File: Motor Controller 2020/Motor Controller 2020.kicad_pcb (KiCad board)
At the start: 2 copper layers, 86 x 60 mm, 49 parts, among them J1 Batt+, J2 Batt-, J3 Input, J4 Motor+, J5 Motor-, Q1 IRF1404, Q2 IRF1404, Q3 IRF1404, Q4 IRF1404, SW1 SW_DIP_x03, U1 MAX15062A, U2 Attiny4313, U3 a4956

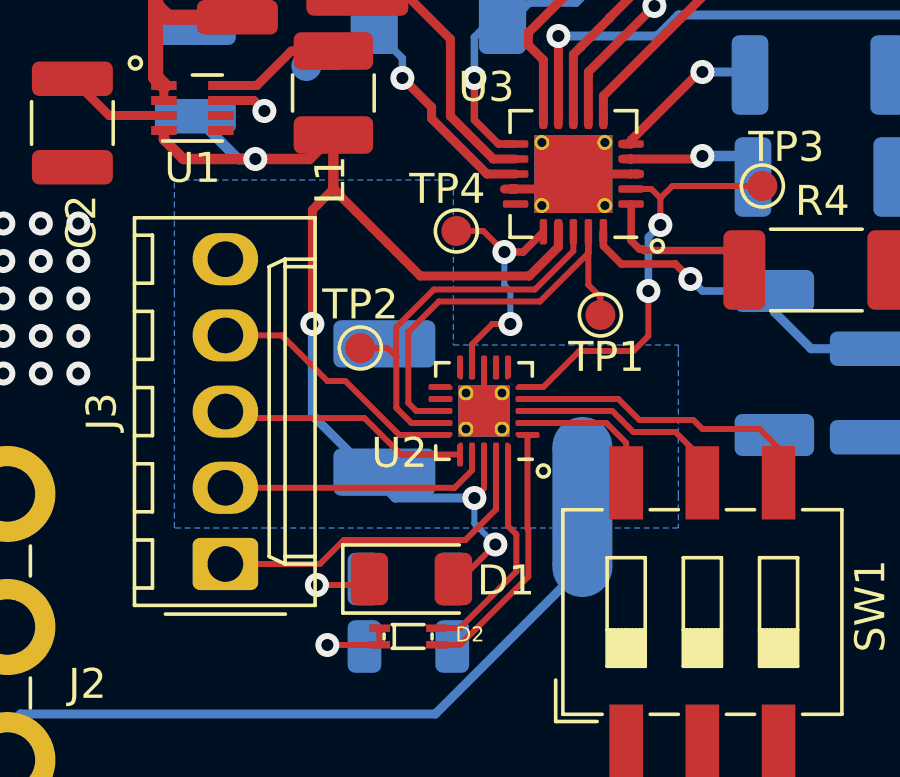
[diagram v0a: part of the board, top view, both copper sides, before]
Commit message: Created new version
Updated PCB and added CRC check for incoming data
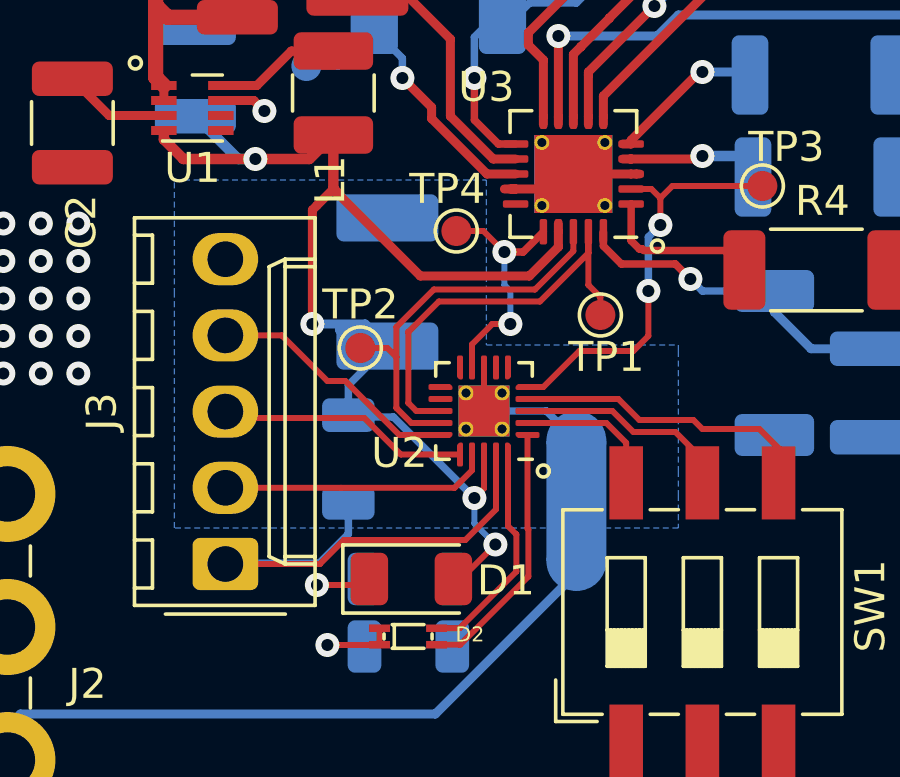
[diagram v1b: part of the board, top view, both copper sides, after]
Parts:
- added R9: 15k, Resistor_SMD:R_1206_3216Metric, B.Cu at (112.7, 89.1)
- moved C7 4.20 mm to (114.0, 83.2)
- moved NT1 0.28 mm to (120.3, 90.5)
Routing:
- net A_RESET: track 11.6 -> 17.2 mm
- net +5V: track 41.5 -> 44.6 mm
- net GNDD: track 4.27 -> 4.94 mm

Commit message: Updated PCB
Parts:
- added R10: 15k, Resistor_SMD:R_1206_3216Metric, F.Cu at (95.0, 61.1)
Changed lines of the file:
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@@
     (tracks 676)
     (zones 0)
-    (modules 50)
+    (modules 51)
     (nets 45)
   )
@@
     (0 F.Cu signal)
     (31 B.Cu signal)
-    (32 B.Adhes user)
-    (33 F.Adhes user)
-    (34 B.Paste user)
-    (35 F.Paste user)
+    (32 B.Adhes user hide)
+    (33 F.Adhes user hide)
+    (34 B.Paste user hide)
+    (35 F.Paste user hide)
     (36 B.SilkS user)
     (37 F.SilkS user)
-    (38 B.Mask user)
-    (39 F.Mask user)
+    (38 B.Mask user hide)
+    (39 F.Mask user hide)
     (40 Dwgs.User user)
     (41 Cmts.User user hide)
@@
     (pad 2 smd roundrect (at 1.4625 0 270) (size 1.125 1.75) (layers B.Cu B.Paste B.Mask) (roundrect_rratio 0.222222)
       (net 17 A_RESET))
+    (model ${KISYS3DMOD}/Resistor_SMD.3dshapes/R_1206_3216Metric.wrl
+      (at (xyz 0 0 0))
+      (scale (xyz 1 1 1))
+      (rotate (xyz 0 0 0))
+    )
+  )
+  (module Resistor_SMD:R_1206_3216Metric (layer F.Cu)
+    (at 95 61.1 270)
+    (descr "Resistor SMD 1206 (3216 Metric), square (rectangular) end terminal, IPC_7351 nominal, (Body size source: IPC-SM-782 page 72, https://www.pcb-3d.com/wordpress/wp-content/uploads/ipc-sm-782a_amendment_1_and_2.pdf), generated with kicad-footprint-generator")
+    (tags resistor)
+    (attr smd)
+    (fp_text reference R10 (at 0 -1.82 90) (layer F.SilkS)
+      (effects (font (size 1 1) (thickness 0.15)))
+    )
+    (fp_text value 15k (at 0 1.82 90) (layer F.Fab)
+      (effects (font (size 1 1) (thickness 0.15)))
+    )
+    (fp_line (start 2.28 1.12) (end -2.28 1.12) (layer F.CrtYd) (width 0.05))
+    (fp_line (start 2.28 -1.12) (end 2.28 1.12) (layer F.CrtYd) (width 0.05))
+    (fp_line (start -2.28 -1.12) (end 2.28 -1.12) (layer F.CrtYd) (width 0.05))
+    (fp_line (start -2.28 1.12) (end -2.28 -1.12) (layer F.CrtYd) (width 0.05))
+    (fp_line (start -0.727064 0.91) (end 0.727064 0.91) (layer F.SilkS) (width 0.12))
+    (fp_line (start -0.727064 -0.91) (end 0.727064 -0.91) (layer F.SilkS) (width 0.12))
+    (fp_line (start 1.6 0.8) (end -1.6 0.8) (layer F.Fab) (width 0.1))
+    (fp_line (start 1.6 -0.8) (end 1.6 0.8) (layer F.Fab) (width 0.1))
+    (fp_line (start -1.6 -0.8) (end 1.6 -0.8) (layer F.Fab) (width 0.1))
+    (fp_line (start -1.6 0.8) (end -1.6 -0.8) (layer F.Fab) (width 0.1))
+    (fp_text user %R (at 0 0 90) (layer F.Fab)
+      (effects (font (size 0.8 0.8) (thickness 0.12)))
+    )
+    (pad 1 smd roundrect (at -1.4625 0 270) (size 1.125 1.75) (layers F.Cu F.Paste F.Mask) (roundrect_rratio 0.222222)
+      (net 26 VCC))
+    (pad 2 smd roundrect (at 1.4625 0 270) (size 1.125 1.75) (layers F.Cu F.Paste F.Mask) (roundrect_rratio 0.222222)
+      (net 1 GND))
     (model ${KISYS3DMOD}/Resistor_SMD.3dshapes/R_1206_3216Metric.wrl
       (at (xyz 0 0 0))
@@
   (segment (start 116.45 93.1) (end 117.6 91.95) (width 0.2) (layer F.Cu) (net 2))
   (segment (start 116.2 93.1) (end 116.45 93.1) (width 0.2) (layer F.Cu) (net 2))
+  (segment (start 113.8 85.4625) (end 113.0625 85.4625) (width 0.3) (layer B.Cu) (net 2))
+  (segment (start 113.0625 85.4625) (end 112.4 84.8) (width 0.3) (layer B.Cu) (net 2))
+  (segment (start 113.2625 84.6) (end 114 85.3375) (width 0.3) (layer B.Cu) (net 2))
+  (segment (start 111.5 84.6) (end 113.2625 84.6) (width 0.3) (layer B.Cu) (net 2))
+  (segment (start 112.7 86.6375) (end 114 85.3375) (width 0.25) (layer B.Cu) (net 2))
+  (segment (start 112.7 87.6375) (end 112.7 86.6375) (width 0.25) (layer B.Cu) (net 2))
+  (segment (start 116.9 90.4) (end 114.2 87.7) (width 0.25) (layer B.Cu) (net 2))
+  (segment (start 112.7625 87.7) (end 112.7 87.6375) (width 0.25) (layer B.Cu) (net 2))
+  (segment (start 114.2 87.7) (end 112.7625 87.7) (width 0.25) (layer B.Cu) (net 2))
   (via (at 144.5 73.7) (size 0.8) (drill 0.4) (layers F.Cu B.Cu) (net 3))
   (via (at 119.7 75) (size 0.8) (drill 0.4) (layers F.Cu B.Cu) (net 3))
@@
   (segment (start 112.55 91.8) (end 116.6 91.8) (width 0.2) (layer F.Cu) (net 17))
   (segment (start 108.6 92.6) (end 111.75 92.6) (width 0.2) (layer F.Cu) (net 17))
+  (segment (start 112.7 90.5625) (end 112.7 91.6) (width 0.25) (layer B.Cu) (net 17))
+  (segment (start 108.625001 92.574999) (end 108.6 92.6) (width 0.25) (layer B.Cu) (net 17))
+  (segment (start 111.725001 92.574999) (end 108.625001 92.574999) (width 0.25) (layer B.Cu) (net 17))
+  (segment (start 112.7 91.6) (end 111.725001 92.574999) (width 0.25) (layer B.Cu) (net 17))
   (via (at 118.1 84.6) (size 0.8) (drill 0.4) (layers F.Cu B.Cu) (net 18))
   (via (at 117.9 82.2) (size 0.8) (drill 0.4) (layers F.Cu B.Cu) (net 18))
@@
   (segment (start 108.45 76.65) (end 109.65 76.65) (width 0.3) (layer F.Cu) (net 22))
   (segment (start 112.2 75.5) (end 110.8 75.5) (width 0.3) (layer F.Cu) (net 22))
-  (segment (start 113.8 85.4625) (end 113.0625 85.4625) (width 0.3) (layer B.Cu) (net 2))
-  (segment (start 113.0625 85.4625) (end 112.4 84.8) (width 0.3) (layer B.Cu) (net 2))
-  (segment (start 113.2625 84.6) (end 114 85.3375) (width 0.3) (layer B.Cu) (net 2))
-  (segment (start 111.5 84.6) (end 113.2625 84.6) (width 0.3) (layer B.Cu) (net 2))
-  (segment (start 112.7 86.6375) (end 114 85.3375) (width 0.25) (layer B.Cu) (net 2))
-  (segment (start 112.7 87.6375) (end 112.7 86.6375) (width 0.25) (layer B.Cu) (net 2))
-  (segment (start 116.9 90.4) (end 114.2 87.7) (width 0.25) (layer B.Cu) (net 2))
-  (segment (start 112.7625 87.7) (end 112.7 87.6375) (width 0.25) (layer B.Cu) (net 2))
-  (segment (start 114.2 87.7) (end 112.7625 87.7) (width 0.25) (layer B.Cu) (net 2))
-  (segment (start 112.7 90.5625) (end 112.7 91.6) (width 0.25) (layer B.Cu) (net 17))
-  (segment (start 108.625001 92.574999) (end 108.6 92.6) (width 0.25) (layer B.Cu) (net 17))
-  (segment (start 111.725001 92.574999) (end 108.625001 92.574999) (width 0.25) (layer B.Cu) (net 17))
-  (segment (start 112.7 91.6) (end 111.725001 92.574999) (width 0.25) (layer B.Cu) (net 17))
   (segment (start 117.221 86.05) (end 117.221 87.5) (width 0.2) (layer F.Cu) (net 25))
   (segment (start 119.300001 87.500001) (end 120.3 88.5) (width 0.25) (layer B.Cu) (net 25))
